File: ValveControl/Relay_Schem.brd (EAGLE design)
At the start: 101.6 x 53.6 mm, 68 parts, among them Q1 LINEAR_REGULATOR, Q2 LINEAR_REGULATOR, Q3 LINEAR_REGULATOR, Q4 LINEAR_REGULATOR, Q5 LINEAR_REGULATOR

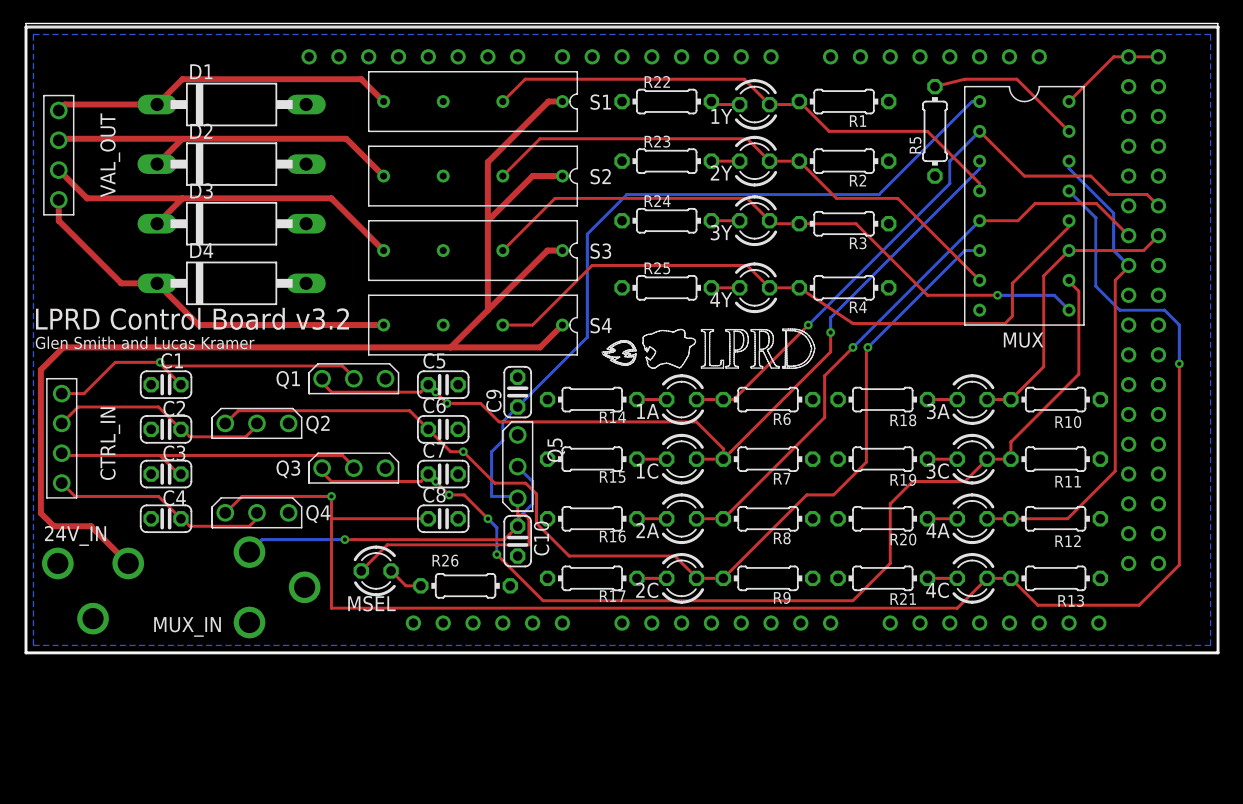
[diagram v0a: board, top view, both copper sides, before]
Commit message: Update schematic for valve board
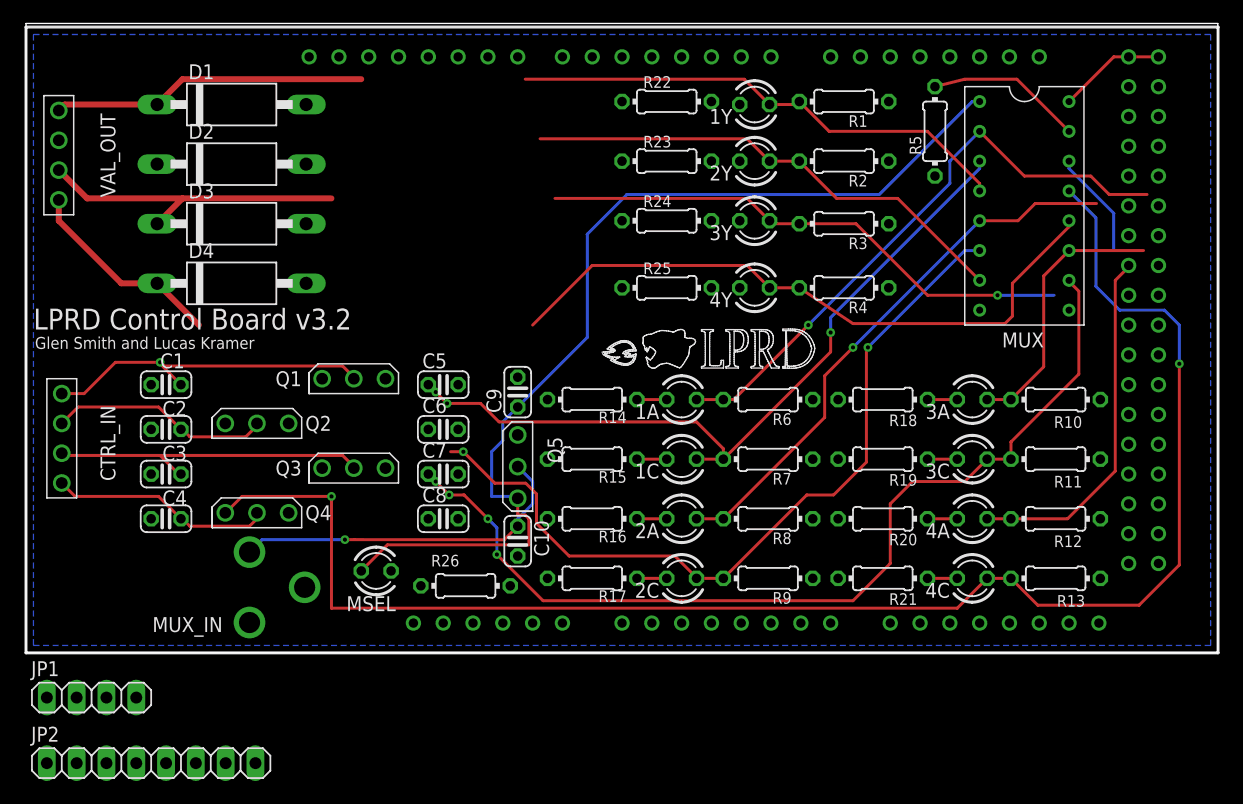
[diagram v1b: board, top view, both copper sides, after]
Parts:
- removed 24V_IN: COAX_POW_2.1MM, LPRD_RELAY:PJ-102A
- removed S1, S2, S3, S4: SSR_CPC1218Y, LPRD_RELAY:CPC1218Y
- added JP1: (no value), pinhead:1X04
- added JP2: (no value), pinhead:1X08
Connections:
- removed net 24V+: 24V_IN.P1, S1.P1, S2.P1, S3.P1, S4.P1
- new net N$25: JP2.1, U$2.27
- new net N$26: JP2.2, U$2.28
- new net N$27: JP2.3, U$2.29
- new net N$28: JP2.4, U$2.30
- new net N$29: JP2.5, U$2.31
- new net N$30: JP2.6, U$2.32
- new net N$31: JP2.7, U$2.33
- new net N$32: JP2.8, U$2.34
- net 0: now also R22.2, R24.2, R25.2, R26.2, U$2.GND@4, U$2.GND@5; no longer 24V_IN.P2, R22.1, R24.1, R25.1, R26.1, S1.P3, S2.P3, S3.P3, S4.P3, U$2.GND@6, U$2.GND@7
- net 1A: now also C5.1, Q1.3; no longer U$2.31
- net 1B: now also JP1.1; no longer C5.1, Q1.3
- net 1Y: no longer S1.P2
- net 2A: now also C6.1, Q2.3; no longer U$2.32
- net 2B: now also JP1.2; no longer C6.1, Q2.3
- net 2Y: no longer S2.P2
- net 3A: now also C7.1, Q3.3; no longer U$2.33
- net 3B: now also JP1.3; no longer C7.1, Q3.3
- net 3Y: no longer S3.P2
- net 4A: now also C8.1, Q4.3; no longer U$2.34
- net 4B: now also JP1.4; no longer C8.1, Q4.3
- net 4Y: no longer S4.P2
- net N$11: now also R22.1; no longer R22.2
- net N$22: now also R24.1; no longer R24.2
- net N$23: now also R25.1; no longer R25.2
- net N$3: no longer S1.P4
- net N$5: no longer S2.P4
- net N$6: now also U$2.5V@2, U$2.5V@3; no longer U$2.GND@4, U$2.GND@5
- net N$7: now also R26.1; no longer R26.2
- net N$8: no longer S3.P4
- net N$9: no longer S4.P4
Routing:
- net 24V+: track 109.5 -> 0.00 mm
- net N$5: track 32.1 -> 0.00 mm
- net 2B: track 89.4 -> 68.3 mm
- net N$9: track 33.1 -> 17.4 mm
- net 3B: track 91.4 -> 80.5 mm
- net 1B: track 75.0 -> 64.1 mm
- net 4B: track 141.1 -> 132.6 mm
- net 3Y: track 54.0 -> 46.0 mm
- net N$8: track 33.6 -> 27.3 mm
- net 2Y: track 47.0 -> 42.5 mm
- net 2A: track 51.2 -> 47.3 mm
- net N$7: track 3.07 -> 0.00 mm
- net N$3: track 29.6 -> 26.9 mm
- net 1Y: track 46.0 -> 43.3 mm
- net 4Y: track 57.6 -> 55.1 mm
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
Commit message: Fix schematic errors, finish board layout
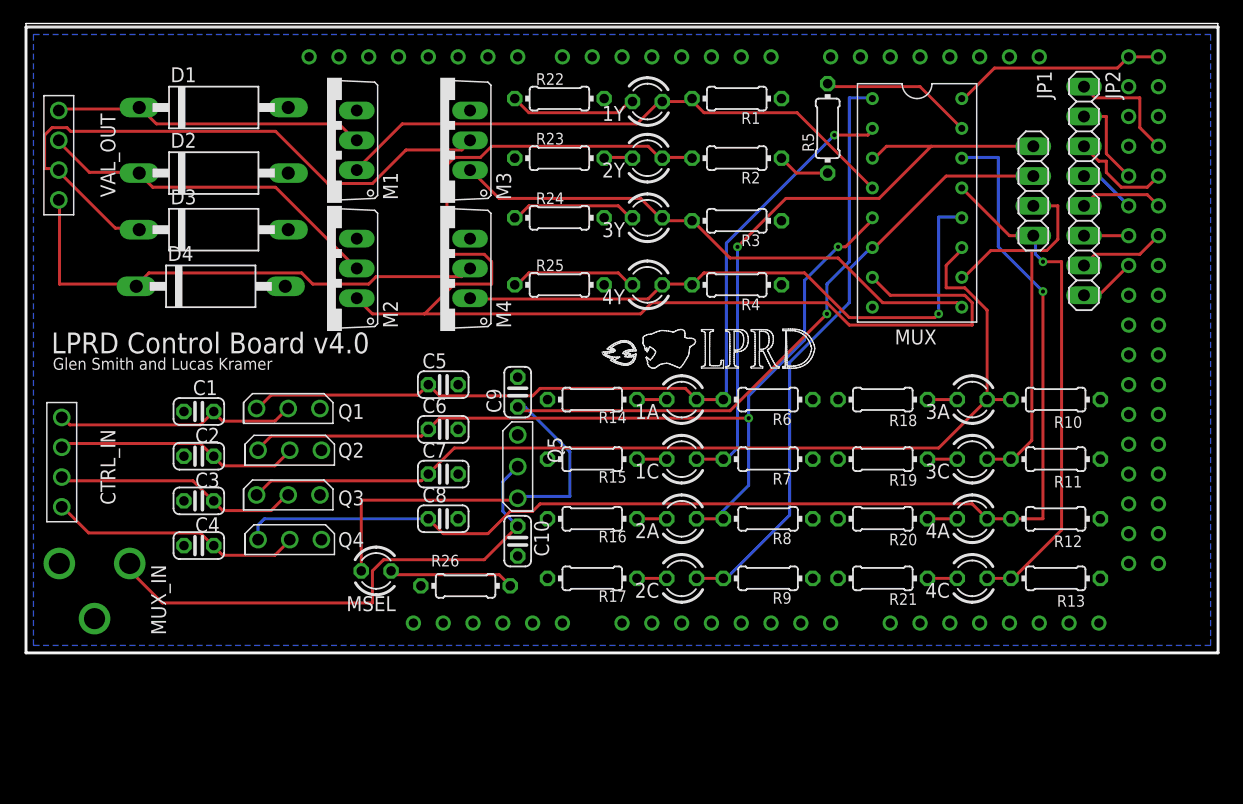
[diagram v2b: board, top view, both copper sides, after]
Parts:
- added M1, M2, M3, M4: IRLZ44, LPRD_RELAY:TO220V
- moved JP2 93.3 mm to (90.2, 39.4), turned to 270 degrees
- moved JP1 91.1 mm to (85.9, 39.4), turned to 270 degrees
- moved MUX_IN 13.4 mm to (5.84, 7.62), turned to 90 degrees
- moved MUX 9.15 mm to (75.9, 38.4)
- moved R5 9.15 mm to (68.3, 44.7)
- moved 1Y 9.15 mm to (53.0, 47.0)
- moved 2Y 9.15 mm to (53.0, 42.2)
- moved 3Y 9.15 mm to (53.0, 37.1)
- moved 4Y 9.15 mm to (53.0, 31.4)
- moved R1 9.15 mm to (60.6, 47.2)
- moved R2 9.15 mm to (60.6, 42.2)
- moved R22 9.15 mm to (45.5, 47.2)
- moved R23 9.15 mm to (45.5, 42.2)
- moved R24 9.15 mm to (45.5, 37.1)
- moved R25 9.15 mm to (45.5, 31.4)
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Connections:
- net 0: now also M1.3, M2.3, M3.3, M4.3
- net 1Y: now also M1.1
- net 2Y: now also M2.1
- net 3Y: now also M3.1
- net 4Y: now also M4.1
- net N$3: now also M1.2
- net N$5: now also M2.2
- net N$8: now also M3.2
- net N$9: now also M4.2
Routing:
- net 4B: track 132.6 -> 43.0 mm, vias 2 -> 1
- net 4A: track 39.7 -> 106.0 mm, vias 0 -> 1
- net 2Y: track 42.5 -> 107.8 mm
- net 3A: track 23.1 -> 83.5 mm
- net 3B: track 80.5 -> 35.1 mm, vias 4 -> 0
- net N$5: track 0.00 -> 30.0 mm
- net 2A: track 47.3 -> 76.6 mm, vias 1 -> 2
- net N$9: track 17.4 -> 43.7 mm
- net N$8: track 27.3 -> 53.2 mm
- net 1A: track 51.2 -> 71.8 mm
- net 2B: track 68.3 -> 52.2 mm, vias 2 -> 0
- net N$24: track 29.9 -> 45.2 mm, vias 1 -> 0
- net N$11: track 0.00 -> 10.9 mm
- net N$23: track 0.00 -> 10.8 mm
- net N$22: track 0.00 -> 10.8 mm
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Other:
- board text added: "LPRD Control Board v4.0"
- board text removed: "LPRD Control Board v3.2"

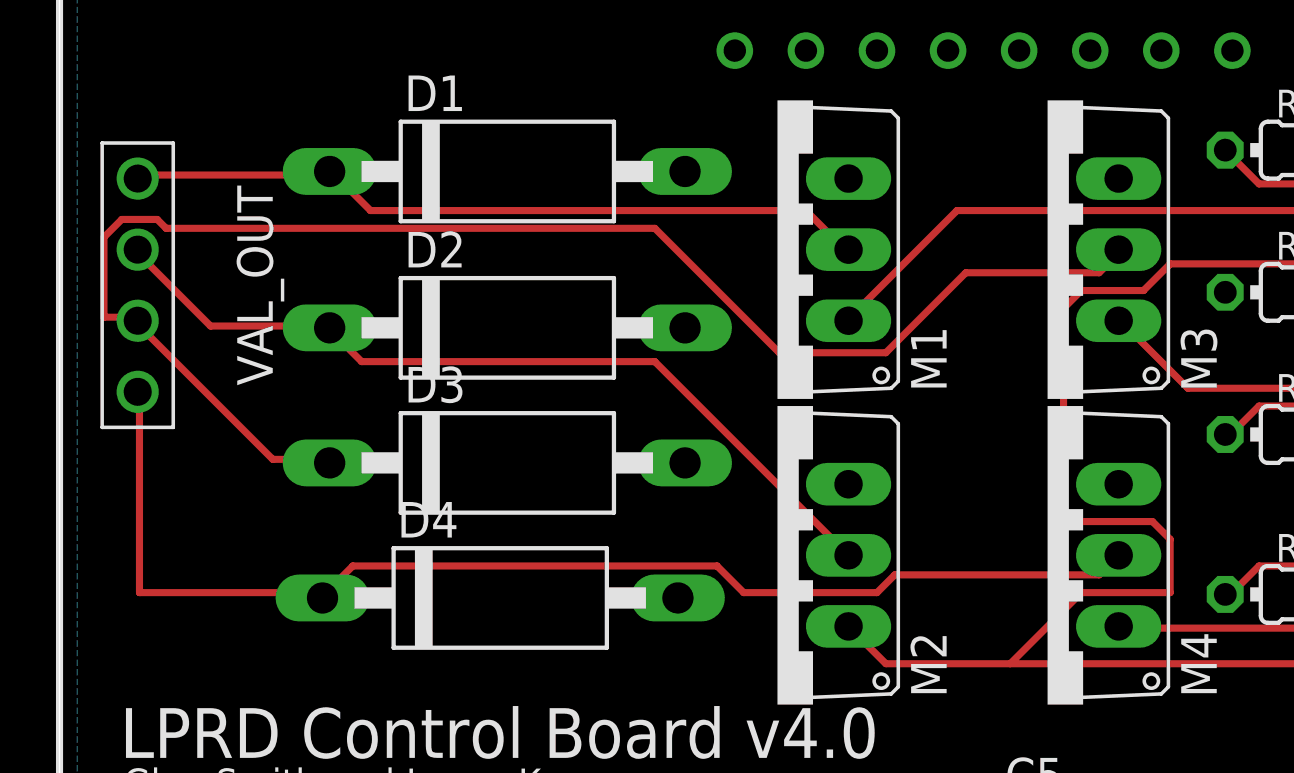
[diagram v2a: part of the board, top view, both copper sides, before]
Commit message: Increase trace width between FET drains and output connector
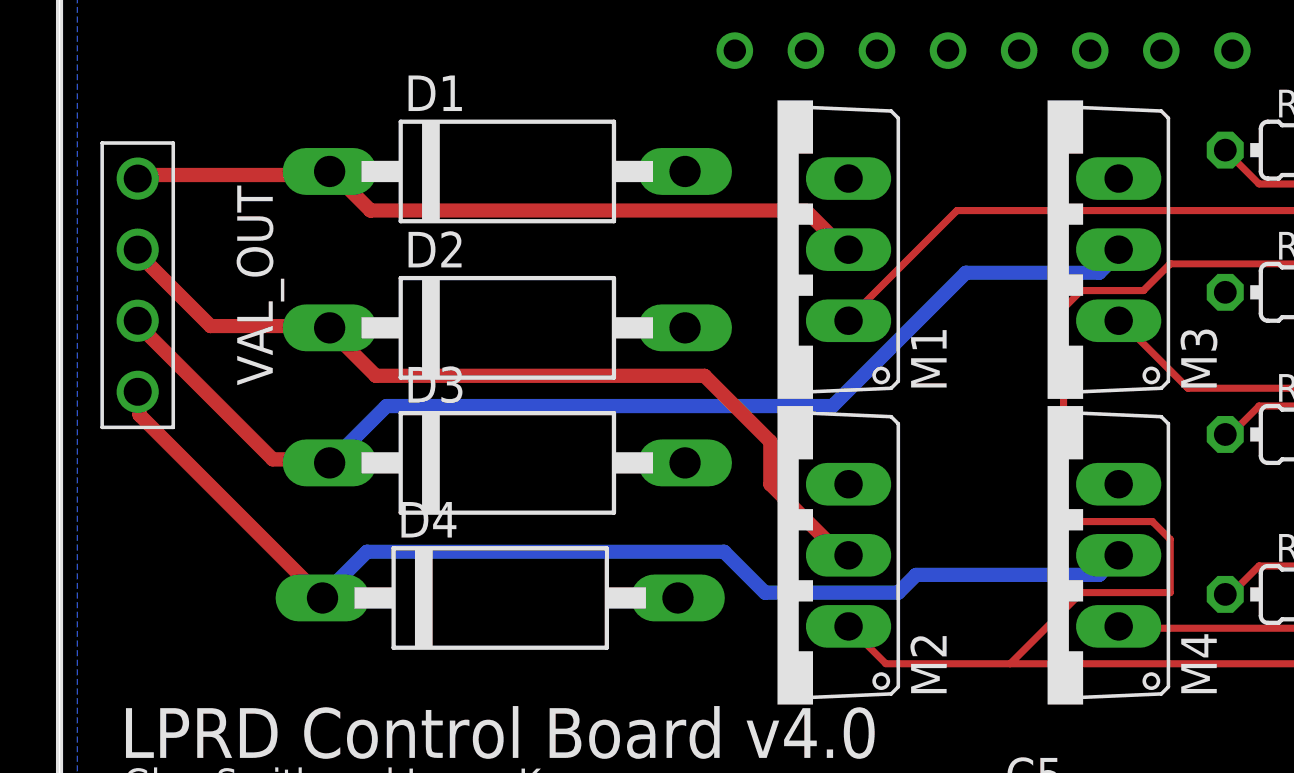
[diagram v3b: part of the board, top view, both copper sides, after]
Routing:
- net N$8: track 53.2 -> 40.4 mm
- net N$9: track 43.7 -> 40.4 mm
- net N$5: track 30.0 -> 30.9 mm
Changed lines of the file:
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@@
 <contactref element="VAL_OUT" pad="P$3"/>
 <contactref element="M3" pad="2"/>
-<wire x1="7.62" y1="36.195" x2="2.8575" y2="40.9575" width="0.254" layer="1"/>
-<wire x1="9.525" y1="36.195" x2="7.62" y2="36.195" width="0.254" layer="1"/>
+<wire x1="7.62" y1="36.195" x2="2.8575" y2="40.9575" width="0.508" layer="1"/>
+<wire x1="9.525" y1="36.195" x2="7.62" y2="36.195" width="0.508" layer="1"/>
 <wire x1="2.8575" y1="40.9575" x2="2.794" y2="41.148" width="0.254" layer="1"/>
-<wire x1="9.525" y1="36.195" x2="9.652" y2="36.068" width="0.254" layer="1"/>
-<wire x1="37.1475" y1="42.8625" x2="37.7825" y2="43.4975" width="0.254" layer="1"/>
-<wire x1="32.385" y1="42.8625" x2="37.1475" y2="42.8625" width="0.254" layer="1"/>
-<wire x1="29.5275" y1="40.005" x2="32.385" y2="42.8625" width="0.254" layer="1"/>
-<wire x1="25.7175" y1="40.005" x2="29.5275" y2="40.005" width="0.254" layer="1"/>
-<wire x1="21.2725" y1="44.45" x2="25.7175" y2="40.005" width="0.254" layer="1"/>
-<wire x1="3.81" y1="44.45" x2="21.2725" y2="44.45" width="0.254" layer="1"/>
-<wire x1="3.4925" y1="44.7675" x2="3.81" y2="44.45" width="0.254" layer="1"/>
-<wire x1="2.2225" y1="44.7675" x2="3.4925" y2="44.7675" width="0.254" layer="1"/>
-<wire x1="1.5875" y1="44.1325" x2="2.2225" y2="44.7675" width="0.254" layer="1"/>
-<wire x1="1.5875" y1="41.275" x2="1.5875" y2="44.1325" width="0.254" layer="1"/>
-<wire x1="2.54" y1="41.275" x2="1.5875" y2="41.275" width="0.254" layer="1"/>
-<wire x1="37.7825" y1="43.4975" x2="37.846" y2="43.688" width="0.254" layer="1"/>
-<wire x1="2.54" y1="41.275" x2="2.794" y2="41.148" width="0.254" layer="1"/>
+<wire x1="9.525" y1="36.195" x2="9.652" y2="36.068" width="0.508" layer="1"/>
+<wire x1="37.1475" y1="42.8625" x2="37.7825" y2="43.4975" width="0.508" layer="16"/>
+<wire x1="37.1475" y1="42.8625" x2="32.385" y2="42.8625" width="0.508" layer="16"/>
+<wire x1="37.7825" y1="43.4975" x2="37.846" y2="43.688" width="0.254" layer="16"/>
+<wire x1="27.6225" y1="38.1" x2="11.684" y2="38.1" width="0.508" layer="16"/>
+<wire x1="11.684" y1="38.1" x2="9.652" y2="36.068" width="0.508" layer="16"/>
+<wire x1="32.385" y1="42.8625" x2="27.6225" y2="38.1" width="0.508" layer="16"/>
 </signal>
 <signal name="N$9">
@@
 <contactref element="VAL_OUT" pad="P$4"/>
 <contactref element="M4" pad="2"/>
-<wire x1="2.8575" y1="31.4325" x2="2.8575" y2="38.4175" width="0.254" layer="1"/>
-<wire x1="9.2075" y1="31.4325" x2="2.8575" y2="31.4325" width="0.254" layer="1"/>
+<wire x1="2.8575" y1="37.7825" x2="2.8575" y2="38.4175" width="0.508" layer="1"/>
 <wire x1="2.8575" y1="38.4175" x2="2.794" y2="38.608" width="0.254" layer="1"/>
-<wire x1="9.2075" y1="31.4325" x2="9.398" y2="31.242" width="0.254" layer="1"/>
-<wire x1="37.1475" y1="32.0675" x2="37.846" y2="32.766" width="0.254" layer="1"/>
-<wire x1="29.845" y1="32.0675" x2="37.1475" y2="32.0675" width="0.254" layer="1"/>
-<wire x1="29.21" y1="31.4325" x2="29.845" y2="32.0675" width="0.254" layer="1"/>
-<wire x1="24.4475" y1="31.4325" x2="29.21" y2="31.4325" width="0.254" layer="1"/>
-<wire x1="23.495" y1="32.385" x2="24.4475" y2="31.4325" width="0.254" layer="1"/>
-<wire x1="10.4775" y1="32.385" x2="23.495" y2="32.385" width="0.254" layer="1"/>
-<wire x1="9.525" y1="31.4325" x2="10.4775" y2="32.385" width="0.254" layer="1"/>
-<wire x1="9.525" y1="31.4325" x2="9.398" y2="31.242" width="0.254" layer="1"/>
+<wire x1="2.8575" y1="37.7825" x2="9.398" y2="31.242" width="0.508" layer="1"/>
+<wire x1="37.1475" y1="32.0675" x2="37.846" y2="32.766" width="0.508" layer="16"/>
+<wire x1="30.607" y1="32.0675" x2="37.1475" y2="32.0675" width="0.508" layer="16"/>
+<wire x1="29.972" y1="31.4325" x2="30.607" y2="32.0675" width="0.508" layer="16"/>
+<wire x1="25.2095" y1="31.4325" x2="29.972" y2="31.4325" width="0.508" layer="16"/>
+<wire x1="23.749" y1="32.893" x2="25.2095" y2="31.4325" width="0.508" layer="16"/>
+<wire x1="10.9855" y1="32.893" x2="23.749" y2="32.893" width="0.508" layer="16"/>
+<wire x1="9.525" y1="31.4325" x2="10.9855" y2="32.893" width="0.508" layer="16"/>
+<wire x1="9.525" y1="31.4325" x2="9.398" y2="31.242" width="0.254" layer="16"/>
 </signal>
 <signal name="N$10">
@@
 <contactref element="VAL_OUT" pad="P$1"/>
 <contactref element="M1" pad="2"/>
-<wire x1="9.525" y1="46.355" x2="2.8575" y2="46.355" width="0.254" layer="1"/>
+<wire x1="9.525" y1="46.355" x2="2.8575" y2="46.355" width="0.508" layer="1"/>
 <wire x1="2.8575" y1="46.355" x2="2.794" y2="46.228" width="0.254" layer="1"/>
 <wire x1="9.525" y1="46.355" x2="9.652" y2="46.482" width="0.254" layer="1"/>
-<wire x1="26.67" y1="45.085" x2="27.94" y2="43.815" width="0.254" layer="1"/>
-<wire x1="11.1125" y1="45.085" x2="26.67" y2="45.085" width="0.254" layer="1"/>
-<wire x1="9.8425" y1="46.355" x2="11.1125" y2="45.085" width="0.254" layer="1"/>
+<wire x1="26.67" y1="45.085" x2="27.94" y2="43.815" width="0.508" layer="1"/>
+<wire x1="11.1125" y1="45.085" x2="26.67" y2="45.085" width="0.508" layer="1"/>
+<wire x1="9.8425" y1="46.355" x2="11.1125" y2="45.085" width="0.508" layer="1"/>
 <wire x1="27.94" y1="43.815" x2="28.194" y2="43.688" width="0.254" layer="1"/>
 <wire x1="9.8425" y1="46.355" x2="9.652" y2="46.482" width="0.254" layer="1"/>
@@
 <contactref element="VAL_OUT" pad="P$2"/>
 <contactref element="M2" pad="2"/>
-<wire x1="5.3975" y1="40.9575" x2="2.8575" y2="43.4975" width="0.254" layer="1"/>
-<wire x1="9.525" y1="40.9575" x2="5.3975" y2="40.9575" width="0.254" layer="1"/>
+<wire x1="5.3975" y1="40.9575" x2="2.8575" y2="43.4975" width="0.508" layer="1"/>
+<wire x1="9.525" y1="40.9575" x2="5.3975" y2="40.9575" width="0.508" layer="1"/>
 <wire x1="2.8575" y1="43.4975" x2="2.794" y2="43.688" width="0.254" layer="1"/>
 <wire x1="9.525" y1="40.9575" x2="9.652" y2="40.894" width="0.254" layer="1"/>
-<wire x1="21.2725" y1="39.6875" x2="28.194" y2="32.766" width="0.254" layer="1"/>
-<wire x1="10.795" y1="39.6875" x2="21.2725" y2="39.6875" width="0.254" layer="1"/>
-<wire x1="9.8425" y1="40.64" x2="10.795" y2="39.6875" width="0.254" layer="1"/>
+<wire x1="25.4" y1="36.83" x2="23.0505" y2="39.1795" width="0.508" layer="1"/>
+<wire x1="25.4" y1="36.83" x2="25.4" y2="35.306" width="0.508" layer="1"/>
+<wire x1="27.94" y1="32.766" x2="25.4" y2="35.306" width="0.508" layer="1"/>
+<wire x1="27.94" y1="32.766" x2="28.194" y2="32.766" width="0.508" layer="1"/>
+<wire x1="11.303" y1="39.1795" x2="23.0505" y2="39.1795" width="0.508" layer="1"/>
+<wire x1="9.8425" y1="40.64" x2="11.303" y2="39.1795" width="0.508" layer="1"/>
 <wire x1="9.8425" y1="40.64" x2="9.652" y2="40.894" width="0.254" layer="1"/>
 </signal>
